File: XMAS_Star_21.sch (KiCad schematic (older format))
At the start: 64 parts, among them J1 USB_B_Micro, J2 Conn_02x01, J3 Conn_02x03_Odd_Even, J4 Conn_01x01_Female, Q1 Q_PMOS_GDS, Q2 FS8205a, SW1 SW_SPDT, U1 ATtiny1607-M, U2 NPIC6C596A, U3 NPIC6C596A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

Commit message: Swapping the shift register for AW9523b
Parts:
- removed U2, U3: NPIC6C596A, UserFootprints:DHVQFN-16_EP_3.6x2.6_Pitch0.5mm, symbol XMAS_Star_21-rescue:NPIC6C596A-UserLibray
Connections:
- wire segments 148 -> 145
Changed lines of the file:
@@
 Text GLabel 8000 5400 2    50   Input ~ 0
 PairZX0
-Wire Wire Line
-	8520 6100 7500 6100
 $Comp
 L Device:LED_ALT D19
@@
 Text GLabel 6800 5800 0    50   Input ~ 0
 SR_Reset_
-Wire Wire Line
-	9100 5300 8520 5300
-Wire Wire Line
-	8520 5300 8520 6100
-$Comp
-L XMAS_Star_21-rescue:NPIC6C596A-UserLibray U2
-U 1 1 5FEFC660
-P 7400 5550
-F 0 "U2" H 7400 5570 50  0000 C CNN
-F 1 "NPIC6C596A" H 7400 5510 50  0000 C CNN
-F 2 "UserFootprints:DHVQFN-16_EP_3.6x2.6_Pitch0.5mm" H 7400 5500 50  0001 C CNN
-F 3 "" H 7400 5500 50  0001 C CNN
-	1    7400 5550
-	1    0    0    -1
-$EndComp
-$Comp
-L XMAS_Star_21-rescue:NPIC6C596A-UserLibray U3
-U 1 1 5FEFD285
-P 9700 5550
-F 0 "U3" H 9700 5580 50  0000 C CNN
-F 1 "NPIC6C596A" H 9700 5520 50  0000 C CNN
-F 2 "UserFootprints:DHVQFN-16_EP_3.6x2.6_Pitch0.5mm" H 9700 5500 50  0001 C CNN
-F 3 "" H 9700 5500 50  0001 C CNN
-	1    9700 5550
-	1    0    0    -1
-$EndComp
 Text GLabel 8000 5300 2    50   Input ~ 0
 SR_CLK

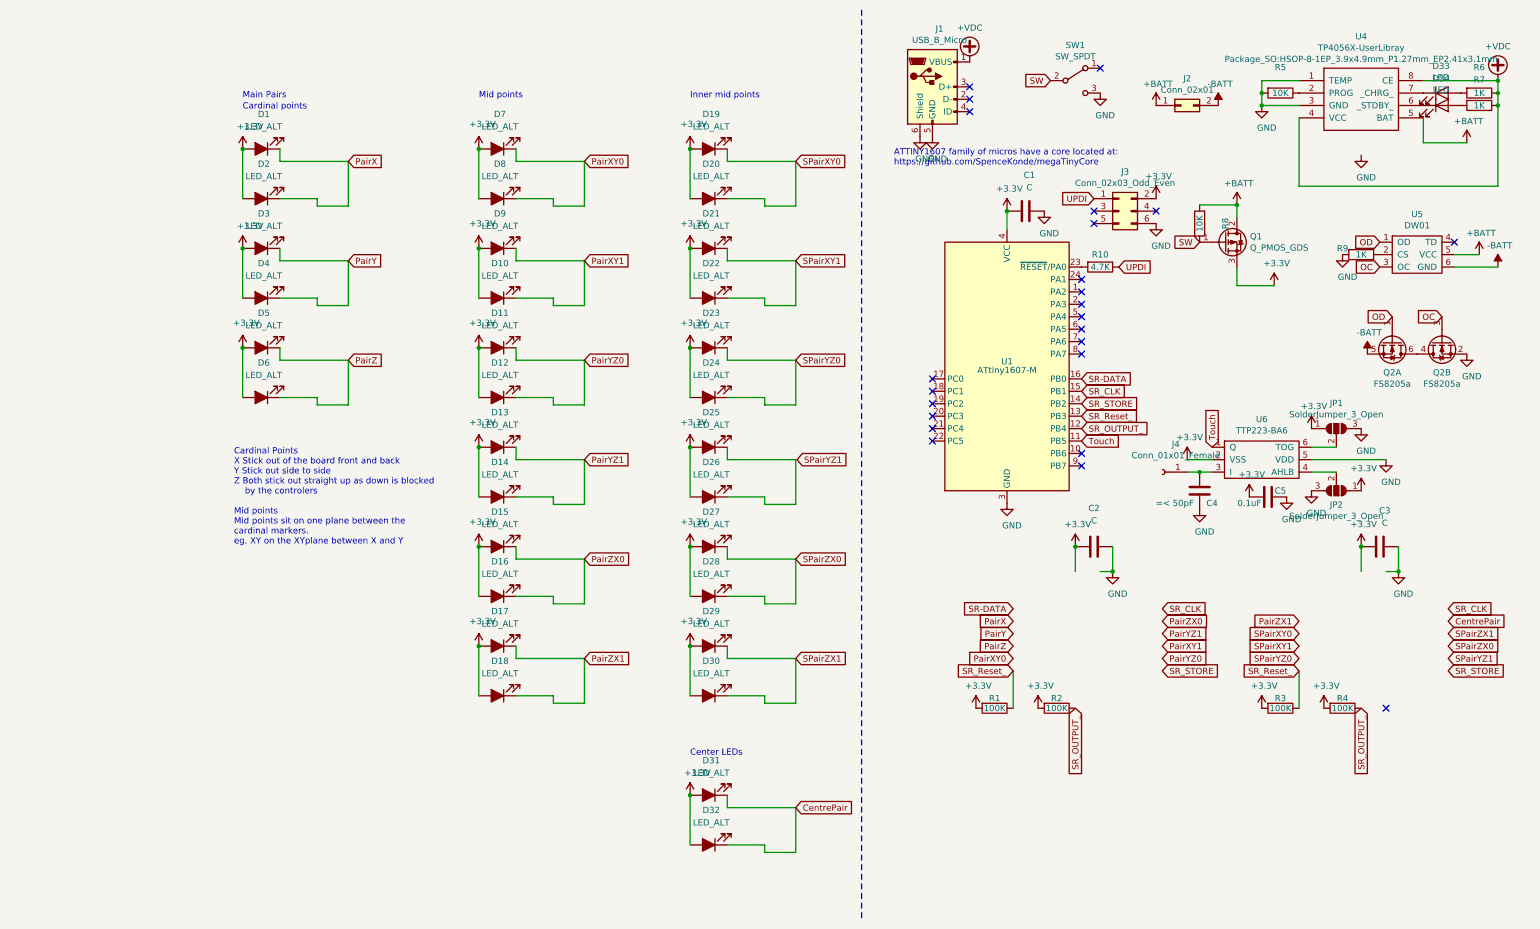
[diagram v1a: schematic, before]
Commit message: Added AW9523b and required nets to schematic
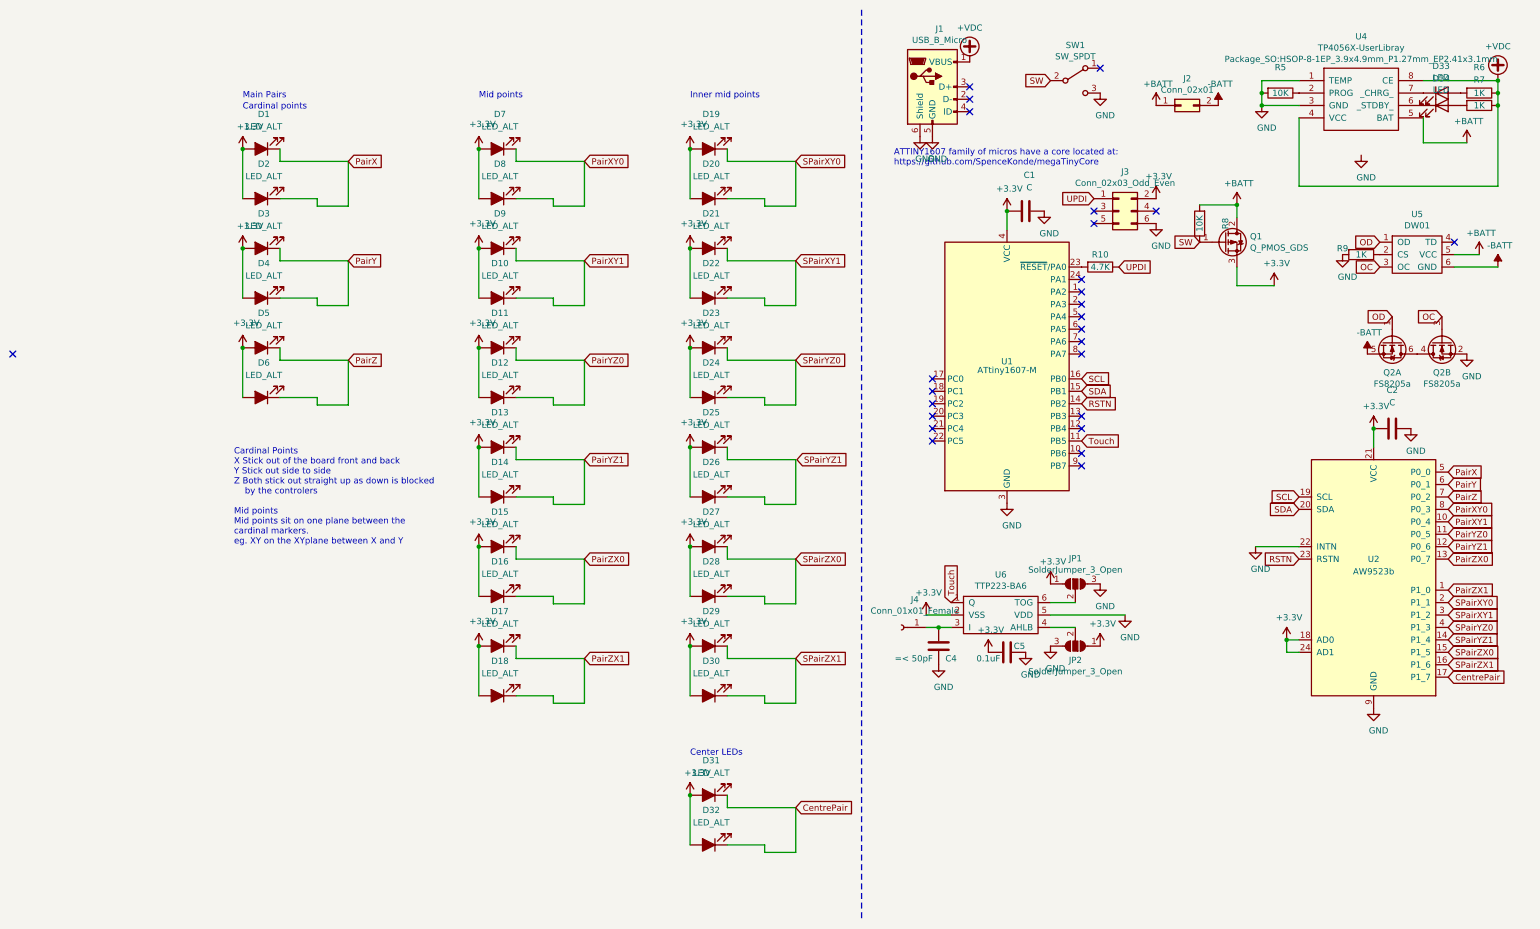
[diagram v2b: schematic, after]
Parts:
- removed C3: C, Capacitor_SMD:C_0603_1608Metric, symbol Device:C
- removed R1, R2, R3, R4: 100K, Resistor_SMD:R_0603_1608Metric, symbol Device:R
- added U2: AW9523b, Package_DFN_QFN:QFN-24-1EP_4x4mm_P0.5mm_EP2.7x2.7mm_ThermalVias, symbol XMAS_Star_21-rescue:AW9523b
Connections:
- net labels added: RSTN, SCL, SDA
- net labels removed: SR-DATA, SR_CLK, SR_OUTPUT_, SR_Reset_, SR_STORE
- wire segments 145 -> 142
- no-connect marks 24 -> 26
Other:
- moved on the sheet: C2, C4, C5, J4, JP1, JP2, U6

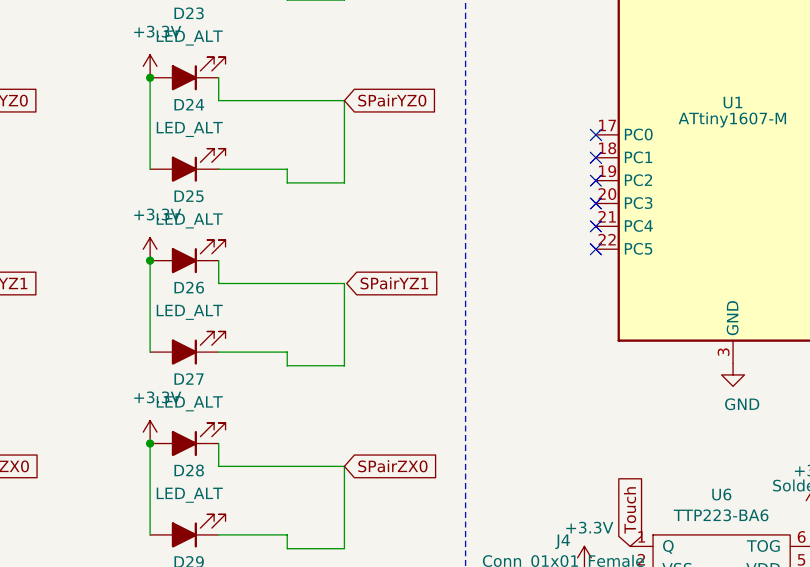
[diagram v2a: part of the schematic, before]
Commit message: Added AW9523b and routing to PCB
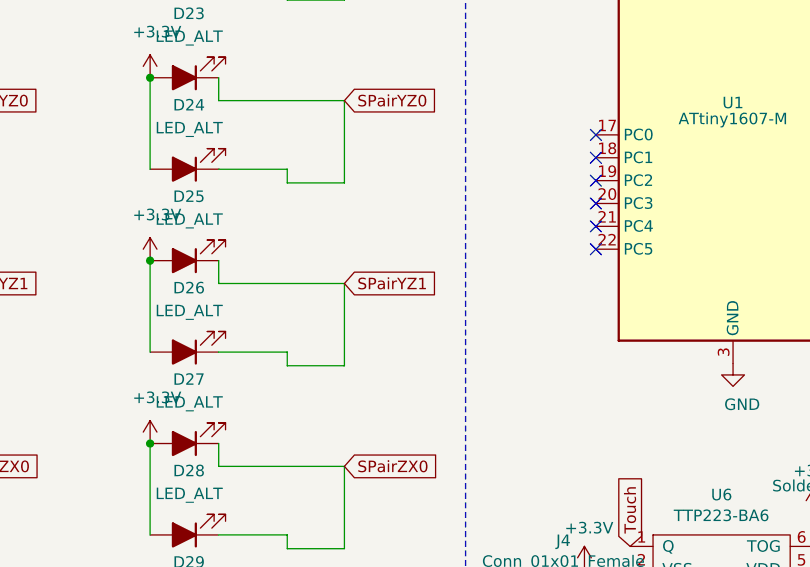
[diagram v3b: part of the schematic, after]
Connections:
- net SPairYZ1: now also D25.1 (K), D26.1 (K)
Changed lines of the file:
@@
 Text GLabel 5050 3300 2    50   Input ~ 0
 SPairYZ0
-Text GLabel 5060 4100 2    50   Input ~ 0
+Text GLabel 5050 4100 2    50   Input ~ 0
 SPairYZ1
 Text GLabel 5050 4900 2    50   Input ~ 0

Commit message: cleaned up UDPI connector
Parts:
- removed J3: Conn_02x03_Odd_Even, Connector_PinSocket_2.54mm:PinSocket_2x03_P2.54mm_Vertical_SMD, symbol Connector_Generic:Conn_02x03_Odd_Even
- added J3: Conn_01x03_Female, Connector_PinSocket_2.54mm:PinSocket_1x03_P2.54mm_Vertical, symbol Connector:Conn_01x03_Female
- J1: symbol Connector:USB_B_Micro -> XMAS_Star_21-rescue:USB_B_Micro-Connector
- U4: symbol X19:TP4056X-UserLibray -> XMAS_Star_21-rescue:TP4056X-UserLibray-X19
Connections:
- net +3V3: now also J3.2 (Pin_2)
- net GND: now also J3.3 (Pin_3)
- net UPDI: now also J3.1 (Pin_1)
- no-connect marks 26 -> 23
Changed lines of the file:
@@
 ATTINY1607 family of micros have a core located at:\nhttps://github.com/SpenceKonde/megaTinyCore\n
 $Comp
-L X19:TP4056X-UserLibray U4
+L XMAS_Star_21-rescue:TP4056X-UserLibray-X19 U4
 U 1 1 5FEBB245
 P 9600 1200
@@
 $EndComp
 $Comp
-L Connector:USB_B_Micro J1
+L XMAS_Star_21-rescue:USB_B_Micro-Connector J1
 U 1 1 5FEBC775
 P 6150 1100
@@
 Connection ~ 6750 2100
 NoConn ~ 6450 1100
-$Comp
-L Connector_Generic:Conn_02x03_Odd_Even J3
-U 1 1 5FEEF18B
-P 7650 2100
-F 0 "J3" H 7700 2417 50  0000 C CNN
-F 1 "Conn_02x03_Odd_Even" H 7700 2326 50  0000 C CNN
-F 2 "Connector_PinSocket_2.54mm:PinSocket_2x03_P2.54mm_Vertical_SMD" H 7650 2100 50  0001 C CNN
-F 3 "~" H 7650 2100 50  0001 C CNN
-	1    7650 2100
-	1    0    0    -1
-$EndComp
-Text GLabel 7450 2000 0    50   Input ~ 0
+Text GLabel 7750 1880 0    50   Input ~ 0
 UPDI
 $Comp
 L power:+3.3V #PWR0111
 U 1 1 5FEF05EB
-P 7950 2000
-F 0 "#PWR0111" H 7950 1850 50  0001 C CNN
-F 1 "+3.3V" H 7970 2180 50  0000 C CNN
-F 2 "" H 7950 2000 50  0001 C CNN
-F 3 "" H 7950 2000 50  0001 C CNN
-	1    7950 2000
+P 7450 1980
+F 0 "#PWR0111" H 7450 1830 50  0001 C CNN
+F 1 "+3.3V" H 7470 2160 50  0000 C CNN
+F 2 "" H 7450 1980 50  0001 C CNN
+F 3 "" H 7450 1980 50  0001 C CNN
+	1    7450 1980
 	1    0    0    -1
 $EndComp
@@
 L power:GND #PWR0112
 U 1 1 5FEF0CBA
-P 7950 2200
-F 0 "#PWR0112" H 7950 1950 50  0001 C CNN
-F 1 "GND" H 7990 2020 50  0000 C CNN
-F 2 "" H 7950 2200 50  0001 C CNN
-F 3 "" H 7950 2200 50  0001 C CNN
-	1    7950 2200
-	1    0    0    -1
-$EndComp
-NoConn ~ 7950 2100
-NoConn ~ 7450 2100
-NoConn ~ 7450 2200
+P 7750 2080
+F 0 "#PWR0112" H 7750 1830 50  0001 C CNN
+F 1 "GND" H 7790 1900 50  0000 C CNN
+F 2 "" H 7750 2080 50  0001 C CNN
+F 3 "" H 7750 2080 50  0001 C CNN
+	1    7750 2080
+	1    0    0    -1
+$EndComp
 $Comp
 L Device:R R10
@@
 NoConn ~ 7350 3750
 NoConn ~ -1250 3250
+$Comp
+L Connector:Conn_01x03_Female J3
+U 1 1 5FF5C419
+P 7950 1980
+F 0 "J3" H 8000 2030 50  0000 L CNN
+F 1 "Conn_01x03_Female" H 8000 1930 50  0000 L CNN
+F 2 "Connector_PinSocket_2.54mm:PinSocket_1x03_P2.54mm_Vertical" H 7950 1980 50  0001 C CNN
+F 3 "~" H 7950 1980 50  0001 C CNN
+	1    7950 1980
+	1    0    0    -1
+$EndComp
+Wire Wire Line
+	7450 1980 7750 1980
 $EndSCHEMATC

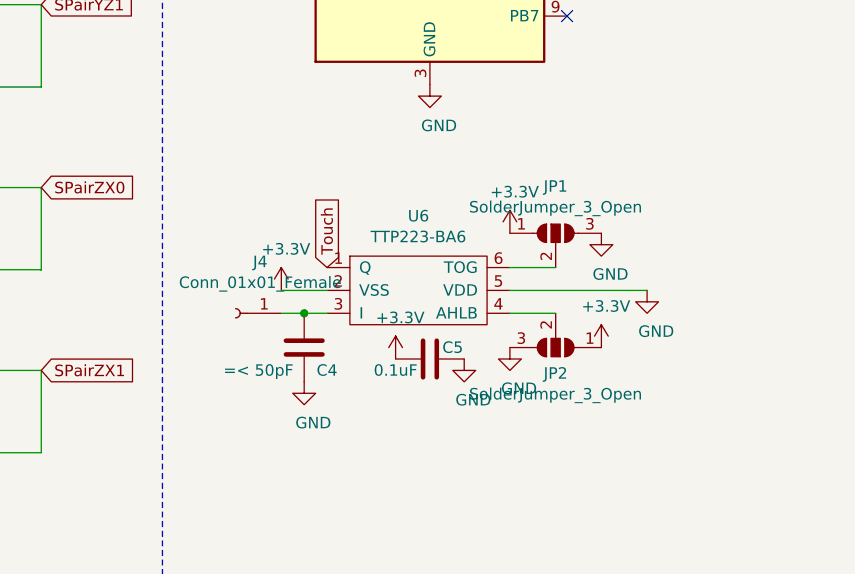
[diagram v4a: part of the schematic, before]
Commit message: tidy power to ICs and start code
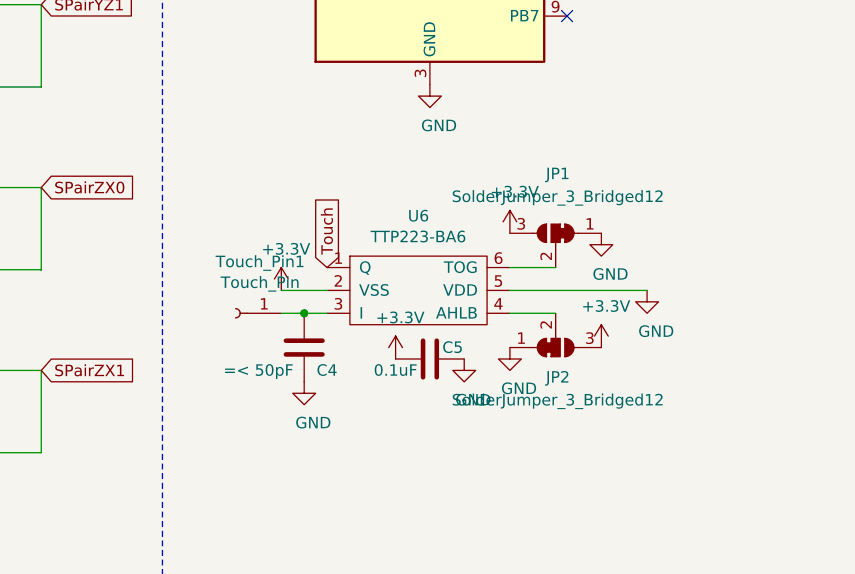
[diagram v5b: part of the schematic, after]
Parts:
- removed JP1, JP2: SolderJumper_3_Open, Jumper:SolderJumper-3_P2.0mm_Open_TrianglePad1.0x1.5mm_NumberLabels, symbol Jumper:SolderJumper_3_Open
- added JP1, JP2: SolderJumper_3_Bridged12, Jumper:SolderJumper-3_P1.3mm_Bridged12_RoundedPad1.0x1.5mm_NumberLabels, symbol Jumper:SolderJumper_3_Bridged12
- Touch_Pin1: renamed from J4; value Conn_01x01_Female -> Touch_Pin
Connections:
- net +3V3: now also JP1.3 (B), JP2.3 (B)
- net GND: now also JP1.1 (A), JP2.1 (A)
- net at U6.4 (AHLB): now also JP2.2 (C)
- net at U6.6 (TOG): now also JP1.2 (C)
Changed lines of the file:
@@
 Touch
 $Comp
-L Connector:Conn_01x01_Female J4
+L Connector:Conn_01x01_Female Touch_Pin1
 U 1 1 5FEF0BA5
 P 5900 5450
-F 0 "J4" H 5792 5225 50  0000 C CNN
-F 1 "Conn_01x01_Female" H 5792 5316 50  0000 C CNN
+F 0 "Touch_Pin1" H 5792 5225 50  0000 C CNN
+F 1 "Touch_Pin" H 5792 5316 50  0000 C CNN
 F 2 "Connector_PinHeader_1.00mm:PinHeader_1x01_P1.00mm_Vertical" H 5900 5450 50  0001 C CNN
 F 3 "~" H 5900 5450 50  0001 C CNN
@@
 	1    6200 5750
 	1    0    0    -1
-$EndComp
-$Comp
-L Jumper:SolderJumper_3_Open JP1
-U 1 1 5FF3E4CD
-P 7300 5100
-F 0 "JP1" H 7300 5305 50  0000 C CNN
-F 1 "SolderJumper_3_Open" H 7300 5214 50  0000 C CNN
-F 2 "Jumper:SolderJumper-3_P2.0mm_Open_TrianglePad1.0x1.5mm_NumberLabels" H 7300 5100 50  0001 C CNN
-F 3 "~" H 7300 5100 50  0001 C CNN
-	1    7300 5100
-	1    0    0    -1
-$EndComp
-$Comp
-L Jumper:SolderJumper_3_Open JP2
-U 1 1 5FF40516
-P 7300 5600
-F 0 "JP2" H 7300 5713 50  0000 C CNN
-F 1 "SolderJumper_3_Open" H 7300 5804 50  0000 C CNN
-F 2 "Jumper:SolderJumper-3_P2.0mm_Open_TrianglePad1.0x1.5mm_NumberLabels" H 7300 5600 50  0001 C CNN
-F 3 "~" H 7300 5600 50  0001 C CNN
-	1    7300 5600
-	-1   0    0    1
 $EndComp
 Wire Wire Line
@@
 Wire Wire Line
 	7450 1980 7750 1980
+$Comp
+L Jumper:SolderJumper_3_Bridged12 JP1
+U 1 1 5FF67DB9
+P 7300 5100
+F 0 "JP1" H 7290 5360 50  0000 C CNN
+F 1 "SolderJumper_3_Bridged12" H 7290 5260 50  0000 C CNN
+F 2 "Jumper:SolderJumper-3_P1.3mm_Bridged12_RoundedPad1.0x1.5mm_NumberLabels" H 7300 5100 50  0001 C CNN
+F 3 "~" H 7300 5100 50  0001 C CNN
+	1    7300 5100
+	-1   0    0    -1
+$EndComp
+$Comp
+L Jumper:SolderJumper_3_Bridged12 JP2
+U 1 1 5FF6A9F7
+P 7300 5600
+F 0 "JP2" H 7310 5730 50  0000 C CNN
+F 1 "SolderJumper_3_Bridged12" H 7310 5830 50  0000 C CNN
+F 2 "Jumper:SolderJumper-3_P1.3mm_Bridged12_RoundedPad1.0x1.5mm_NumberLabels" H 7300 5600 50  0001 C CNN
+F 3 "~" H 7300 5600 50  0001 C CNN
+	1    7300 5600
+	1    0    0    1
+$EndComp
 $EndSCHEMATC

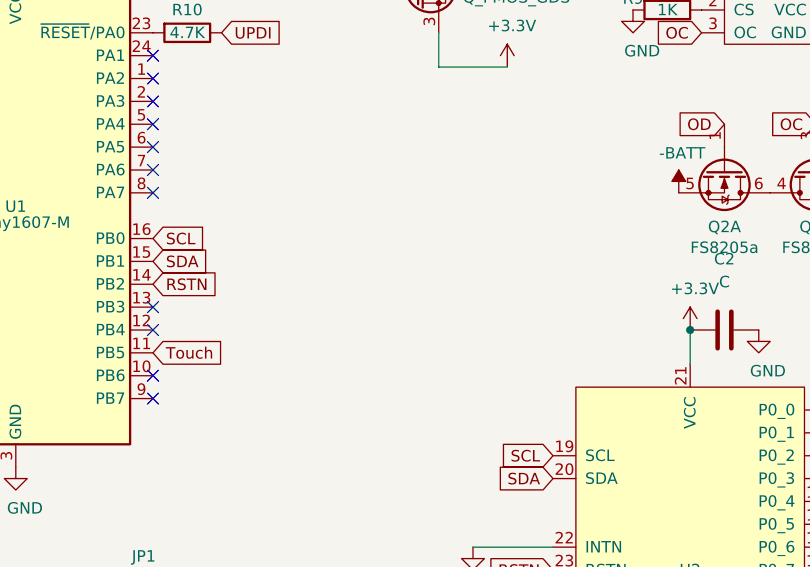
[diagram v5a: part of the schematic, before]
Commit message: Remembering to put pullups on the i2cgit add --all
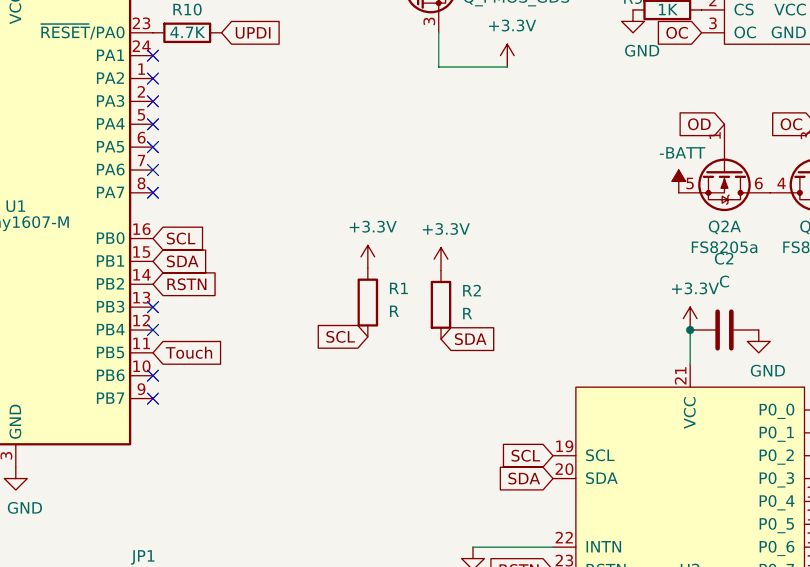
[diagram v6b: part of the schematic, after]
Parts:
- added R1, R2: R, Resistor_SMD:R_0603_1608Metric, symbol Device:R
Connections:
- net +3V3: now also R1.1, R2.1
- net SCL: now also R1.2
- net SDA: now also R2.2
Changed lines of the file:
@@
 	1    0    0    1
 $EndComp
+$Comp
+L Device:R R1
+U 1 1 5FF7D209
+P 8290 3730
+F 0 "R1" H 8380 3790 50  0000 L CNN
+F 1 "R" H 8380 3690 50  0000 L CNN
+F 2 "Resistor_SMD:R_0603_1608Metric" V 8220 3730 50  0001 C CNN
+F 3 "~" H 8290 3730 50  0001 C CNN
+	1    8290 3730
+	1    0    0    -1
+$EndComp
+$Comp
+L Device:R R2
+U 1 1 5FF7DC22
+P 8610 3740
+F 0 "R2" H 8700 3800 50  0000 L CNN
+F 1 "R" H 8700 3700 50  0000 L CNN
+F 2 "Resistor_SMD:R_0603_1608Metric" V 8540 3740 50  0001 C CNN
+F 3 "~" H 8610 3740 50  0001 C CNN
+	1    8610 3740
+	1    0    0    -1
+$EndComp
+Text GLabel 8290 3880 0    50   Input ~ 0
+SCL
+Text GLabel 8610 3890 2    50   Input ~ 0
+SDA
+$Comp
+L power:+3.3V #PWR0113
+U 1 1 5FF7E430
+P 8290 3580
+F 0 "#PWR0113" H 8290 3430 50  0001 C CNN
+F 1 "+3.3V" H 8310 3760 50  0000 C CNN
+F 2 "" H 8290 3580 50  0001 C CNN
+F 3 "" H 8290 3580 50  0001 C CNN
+	1    8290 3580
+	1    0    0    -1
+$EndComp
+$Comp
+L power:+3.3V #PWR0114
+U 1 1 5FF7F85C
+P 8610 3590
+F 0 "#PWR0114" H 8610 3440 50  0001 C CNN
+F 1 "+3.3V" H 8630 3770 50  0000 C CNN
+F 2 "" H 8610 3590 50  0001 C CNN
+F 3 "" H 8610 3590 50  0001 C CNN
+	1    8610 3590
+	1    0    0    -1
+$EndComp
 $EndSCHEMATC
